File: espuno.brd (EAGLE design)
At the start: 68.6 x 53.3 mm, 62 parts, among them J1 ARDUINO_R3_SHIELD, T1 FDN340P, U1 ADS1115IDGST, U2 NCP1117ST50T3G, U3 LP2985-33DBVR, U4 FT232R, U5 LMV358IDGKR, U6 MCP73831, U7 TPS61200, X1 POWERSUPPLY_DC21MMX

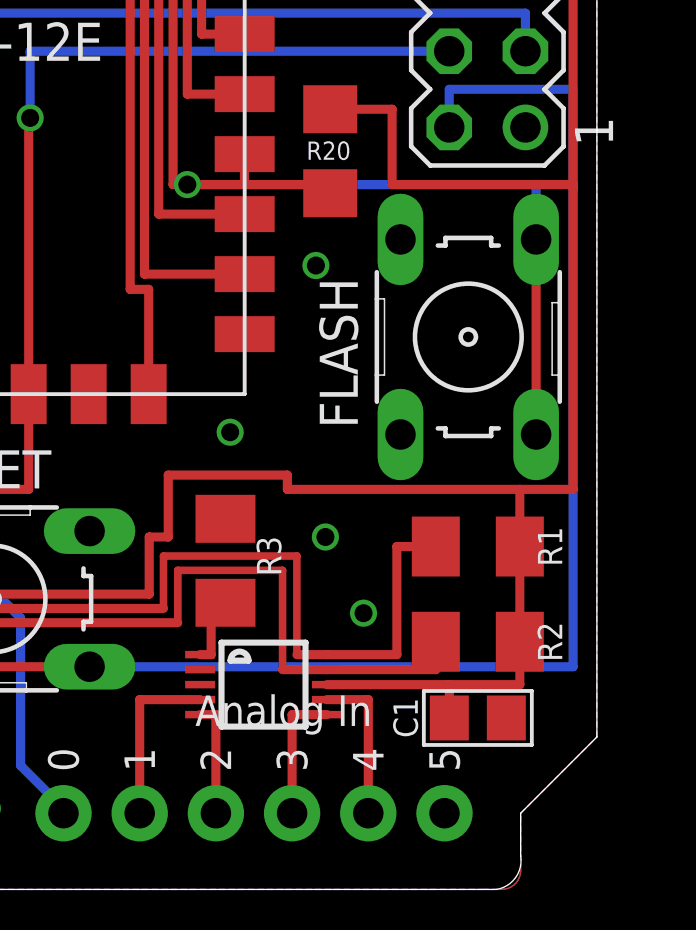
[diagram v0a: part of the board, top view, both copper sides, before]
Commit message: Revise which size C1 is
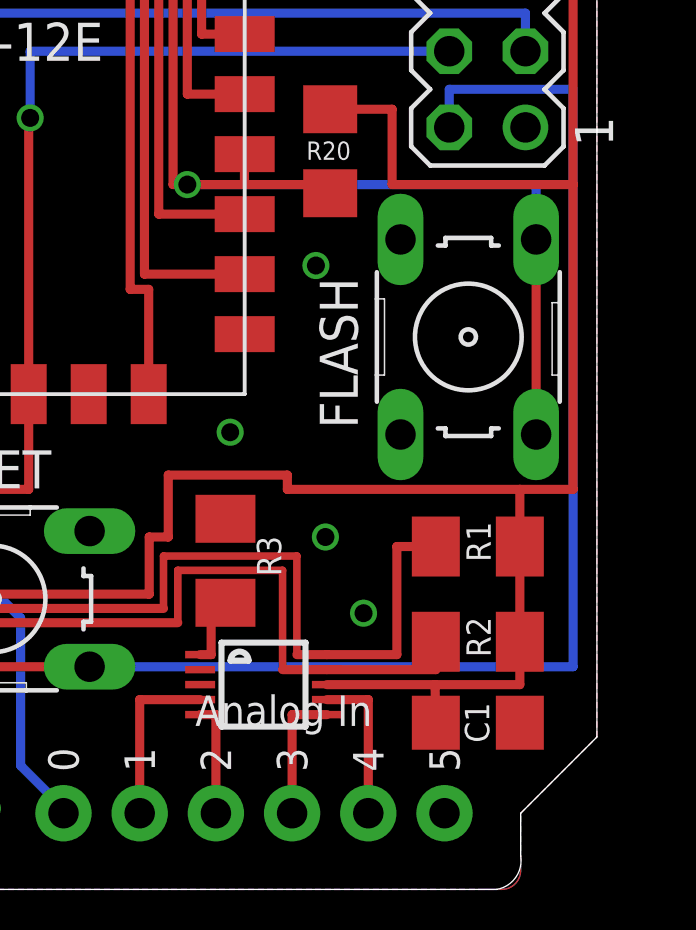
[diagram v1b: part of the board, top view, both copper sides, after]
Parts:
- C1: device microbuilder:0805 -> SparkFun-Capacitors:1206
- moved C1 0.16 mm to (64.6, 5.56)
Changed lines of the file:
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@@
 <element name="MDL1" library="ESP8266-ESP12E" package="ESP8266-ESP12E" value="" x="40.64" y="16.51" smashed="yes"/>
 <element name="U1" library="microbuilder" package="MSOP10" value="ADS1115IDGST" x="57.4675" y="6.82625" smashed="yes" rot="R270"/>
-<element name="C1" library="microbuilder" package="0805" value="1µF" x="64.61125" y="5.715" smashed="yes" rot="R180">
-<attribute name="NAME" x="62.611" y="5.04825" size="0.8128" layer="25" rot="R90"/>
+<element name="C1" library="SparkFun-Capacitors" package="1206" value="1µF" x="64.61125" y="5.55625" smashed="yes" rot="R180">
+<attribute name="NAME" x="64.99225" y="4.8895" size="0.8128" layer="25" rot="R90"/>
 </element>
 <element name="R1" library="rcl" package="M1206" value="10K" x="64.61125" y="11.43" smashed="yes" rot="R180">
-<attribute name="NAME" x="66.6115" y="12.09675" size="0.8128" layer="25" rot="R270"/>
+<attribute name="NAME" x="64.23025" y="12.2555" size="0.8128" layer="25" rot="R270"/>
 </element>
 <element name="R2" library="rcl" package="M1206" value="10K" x="64.61125" y="8.255" smashed="yes" rot="R180">
-<attribute name="NAME" x="66.6115" y="8.92175" size="0.8128" layer="25" rot="R270"/>
+<attribute name="NAME" x="64.23025" y="9.0805" size="0.8128" layer="25" rot="R270"/>
 </element>
 <element name="R3" library="rcl" package="M1206" value="10K" x="56.1975" y="10.95375" smashed="yes" rot="R90">
@@
 <wire x1="36.425" y1="14.2875" x2="36.35375" y2="14.44625" width="0.3048" layer="1"/>
 <wire x1="36.35375" y1="14.44625" x2="36.35375" y2="12.54125" width="0.3048" layer="1"/>
-<wire x1="59.5806" y1="6.82625" x2="63.66125" y2="6.82625" width="0.3048" layer="1"/>
-<wire x1="63.66125" y1="6.82625" x2="63.66125" y2="5.715" width="0.3048" layer="1"/>
+<wire x1="59.5806" y1="6.82625" x2="63.185" y2="6.82625" width="0.3048" layer="1"/>
+<wire x1="63.185" y1="6.82625" x2="63.21125" y2="5.55625" width="0.3048" layer="1"/>
 <wire x1="66.01125" y1="8.255" x2="66.01125" y2="6.82625" width="0.3048" layer="1"/>
-<wire x1="66.01125" y1="6.82625" x2="63.66125" y2="6.82625" width="0.3048" layer="1"/>
+<wire x1="66.01125" y1="6.82625" x2="63.185" y2="6.82625" width="0.3048" layer="1"/>
 <wire x1="66.01125" y1="11.43" x2="66.01125" y2="8.255" width="0.3048" layer="1"/>
 <wire x1="24.1215" y1="21.85825" x2="24.1215" y2="25.0825" width="0.3048" layer="1"/>
@@
 <wire x1="66.19875" y1="30.48" x2="67.78625" y2="30.48" width="0.3048" layer="1"/>
 <wire x1="67.78625" y1="30.48" x2="67.78625" y2="23.495" width="0.3048" layer="1"/>
-<wire x1="67.78625" y1="23.33625" x2="67.78625" y2="13.335" width="0.3048" layer="1"/>
+<wire x1="67.78625" y1="23.495" x2="67.78625" y2="13.335" width="0.3048" layer="1"/>
 <wire x1="67.78625" y1="13.335" x2="66.01125" y2="13.335" width="0.3048" layer="1"/>
 <contactref element="R20" pad="1"/>
@@
 <wire x1="61.75375" y1="26.00625" x2="61.75375" y2="23.495" width="0.3048" layer="1"/>
 <wire x1="61.75375" y1="23.495" x2="67.78625" y2="23.495" width="0.3048" layer="1"/>
-<wire x1="67.78625" y1="23.495" x2="67.78625" y2="23.33625" width="0.3048" layer="1"/>
 </signal>
 <signal name="GND">

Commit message: Change 100nf => 0.1uf
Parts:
- C1: value 1µF -> 0.1uf
- C2, C3: value 100n -> 0.1uf
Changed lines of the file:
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@@
 <element name="MDL1" library="ESP8266-ESP12E" package="ESP8266-ESP12E" value="" x="40.64" y="16.51" smashed="yes"/>
 <element name="U1" library="microbuilder" package="MSOP10" value="ADS1115IDGST" x="57.4675" y="6.82625" smashed="yes" rot="R270"/>
-<element name="C1" library="SparkFun-Capacitors" package="1206" value="1µF" x="64.61125" y="5.55625" smashed="yes" rot="R180">
+<element name="C1" library="SparkFun-Capacitors" package="1206" value="0.1uf" x="64.61125" y="5.55625" smashed="yes" rot="R180">
 <attribute name="NAME" x="64.99225" y="4.8895" size="0.8128" layer="25" rot="R90"/>
 </element>
@@
 <attribute name="NAME" x="57.24525" y="11.77925" size="0.8128" layer="25" rot="R270"/>
 </element>
-<element name="C2" library="rcl" package="C1206K" value="100n" x="40.64" y="9.36625" smashed="yes" rot="R270">
+<element name="C2" library="rcl" package="C1206K" value="0.1uf" x="40.64" y="9.36625" smashed="yes" rot="R270">
 <attribute name="NAME" x="40.0685" y="9.017" size="0.6096" layer="25"/>
 </element>
@@
 </element>
 <element name="T1" library="zetex" package="SOT-23" value="FDN340P" x="28.575" y="17.4625" smashed="yes" rot="R90"/>
-<element name="C3" library="rcl" package="C1206K" value="100n" x="38.1" y="9.36625" smashed="yes" rot="R270">
+<element name="C3" library="rcl" package="C1206K" value="0.1uf" x="38.1" y="9.36625" smashed="yes" rot="R270">
 <attribute name="NAME" x="37.5285" y="9.17575" size="0.6096" layer="25"/>
 </element>

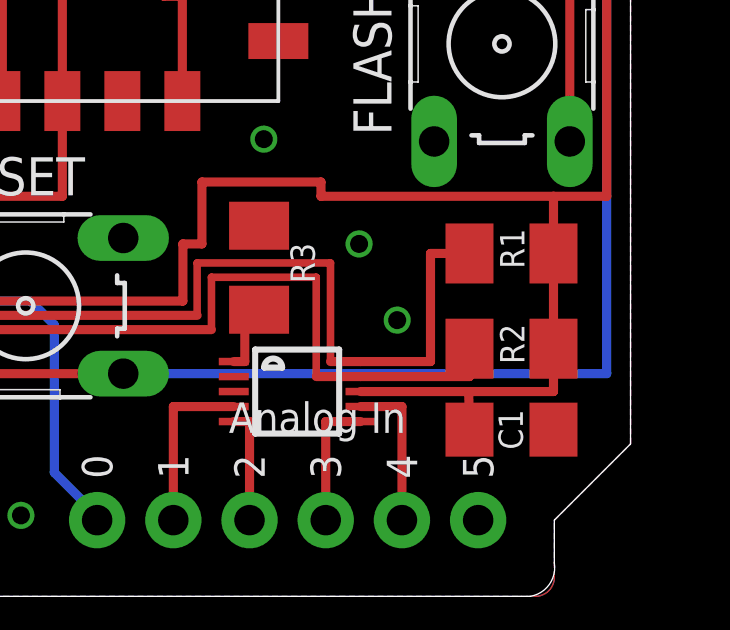
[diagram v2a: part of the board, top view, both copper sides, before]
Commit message: Move i2c pullup resistors to Pullups section of schematic
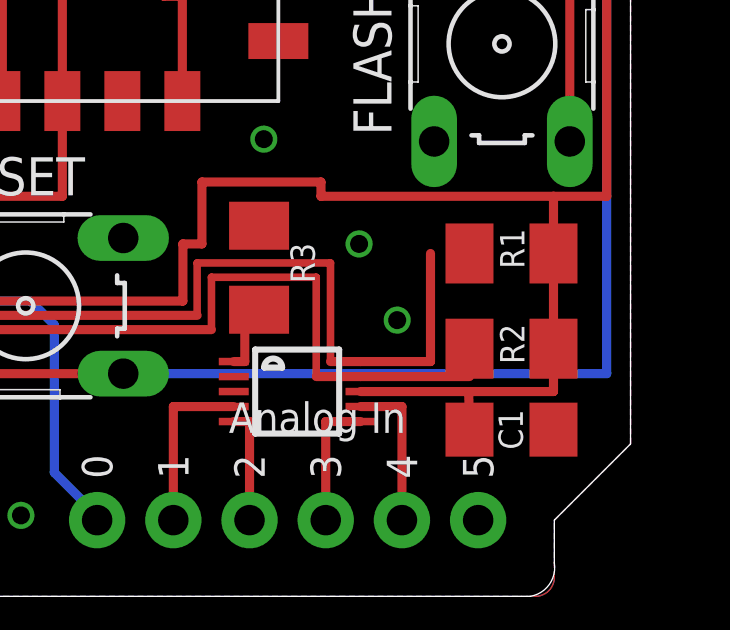
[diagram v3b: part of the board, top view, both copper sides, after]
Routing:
- net SCL/GPIO14: track 88.7 -> 87.4 mm
- net SDA/GPIO16: track 87.2 -> 86.3 mm
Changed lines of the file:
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@@
 <contactref element="MDL1" pad="4"/>
 <contactref element="U1" pad="9"/>
-<contactref element="R2" pad="2"/>
 <contactref element="J1" pad="SDA"/>
 <wire x1="59.5806" y1="7.32625" x2="63.21125" y2="7.32625" width="0.3048" layer="1"/>
-<wire x1="63.21125" y1="7.32625" x2="63.21125" y2="8.255" width="0.3048" layer="1"/>
 <wire x1="21.59" y1="50.8" x2="32.54375" y2="39.84625" width="0.3048" layer="1"/>
 <wire x1="32.54375" y1="39.84625" x2="32.54375" y2="30.32125" width="0.3048" layer="1"/>
@@
 <via x="42.70375" y="8.09625" extent="1-16" drill="0.6"/>
 <wire x1="42.70375" y1="8.09625" x2="40.79875" y2="10.00125" width="0.3048" layer="16"/>
+<contactref element="R2" pad="2"/>
+<wire x1="63.21125" y1="7.32625" x2="63.21125" y2="8.255" width="0" layer="19" extent="1-1"/>
 </signal>
 <signal name="SCL/GPIO14">
 <contactref element="MDL1" pad="5"/>
 <contactref element="U1" pad="10"/>
-<contactref element="R1" pad="2"/>
 <contactref element="J1" pad="SCL"/>
 <wire x1="59.5806" y1="7.82625" x2="61.9125" y2="7.82625" width="0.3048" layer="1"/>
 <wire x1="61.9125" y1="7.82625" x2="61.9125" y2="11.43" width="0.3048" layer="1"/>
-<wire x1="61.9125" y1="11.43" x2="63.21125" y2="11.43" width="0.3048" layer="1"/>
 <wire x1="19.05" y1="50.8" x2="32.0675" y2="37.7825" width="0.3048" layer="1"/>
 <wire x1="32.0675" y1="37.7825" x2="32.0675" y2="26.82875" width="0.3048" layer="1"/>
@@
 <via x="42.70375" y="9.36625" extent="1-16" drill="0.6"/>
 <wire x1="42.70375" y1="9.36625" x2="54.13375" y2="9.36625" width="0.3048" layer="1"/>
+<contactref element="R1" pad="2"/>
+<wire x1="61.9125" y1="11.43" x2="63.21125" y2="11.43" width="0" layer="19" extent="1-1"/>
 </signal>
 <signal name="ADDR">
